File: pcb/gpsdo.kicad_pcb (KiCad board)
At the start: 4 copper layers, 140 x 100 mm, 159 parts, among them IC1 ICE40LP384-SG32, J1 JTAG, J10 CLK0, J11 CLK7, J12 USB_B_Micro, J13 CLK6, J14 CLK5, J15 CLK4, J2 SSD1306, J3 EXT_CLOCK, J4 GPS_ANT, J5 USB_B_Micro, J6 CLK3, J7 Screw_Terminal_01x03, J8 CLK2, J9 CLK1, M1 E73-2G4M08S1C-52840, Q1 S9018, SW1 EC11, SW2 MCML4-112B, U1 MCP9808_MSOP, U2 MCP9808_MSOP, U3 TPS652510, U4 LT1763xS8, U5 74LVC1G17, U6 Si5351C-B-GM, U7 74LVC1G17, U8 uBlox NEO-7M, U9 AD5761R, Y1 32768, Y2 8663-XS

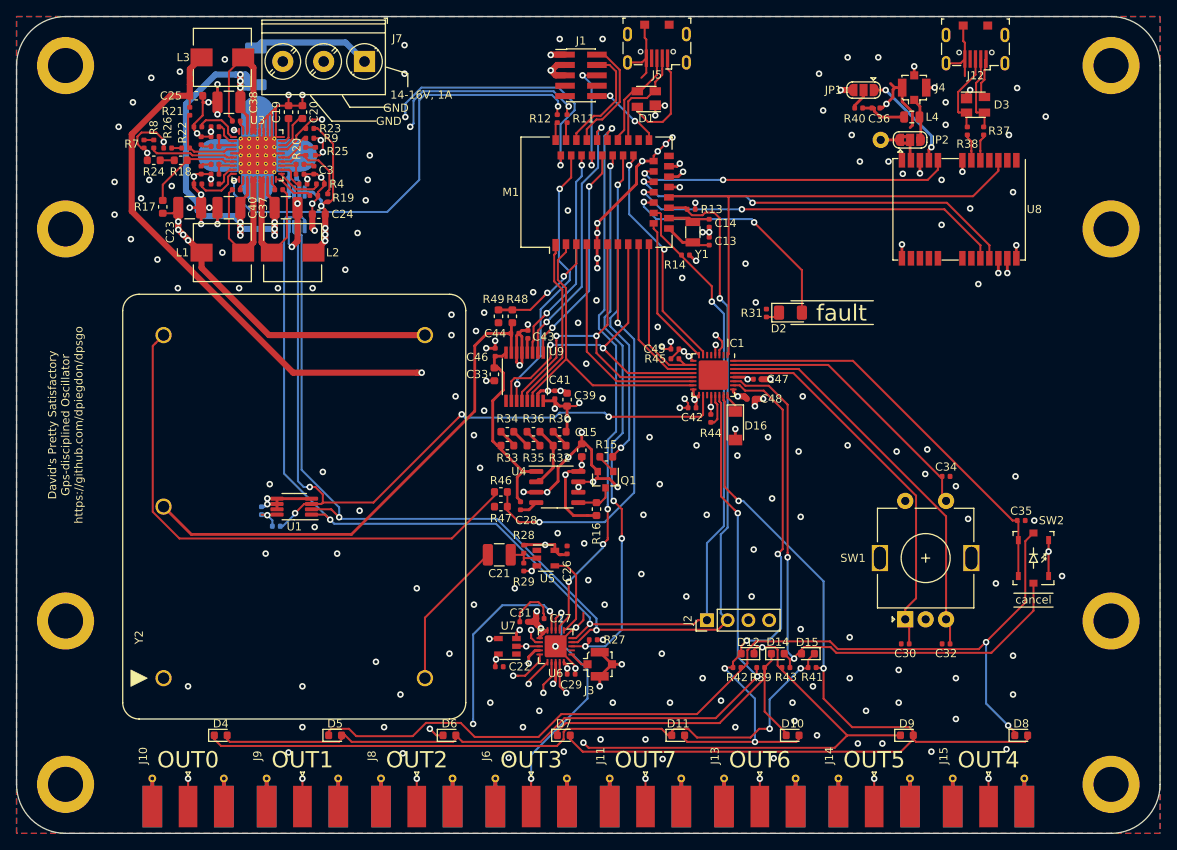
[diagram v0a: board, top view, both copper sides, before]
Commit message: added shield and more silkscreen, cleanup
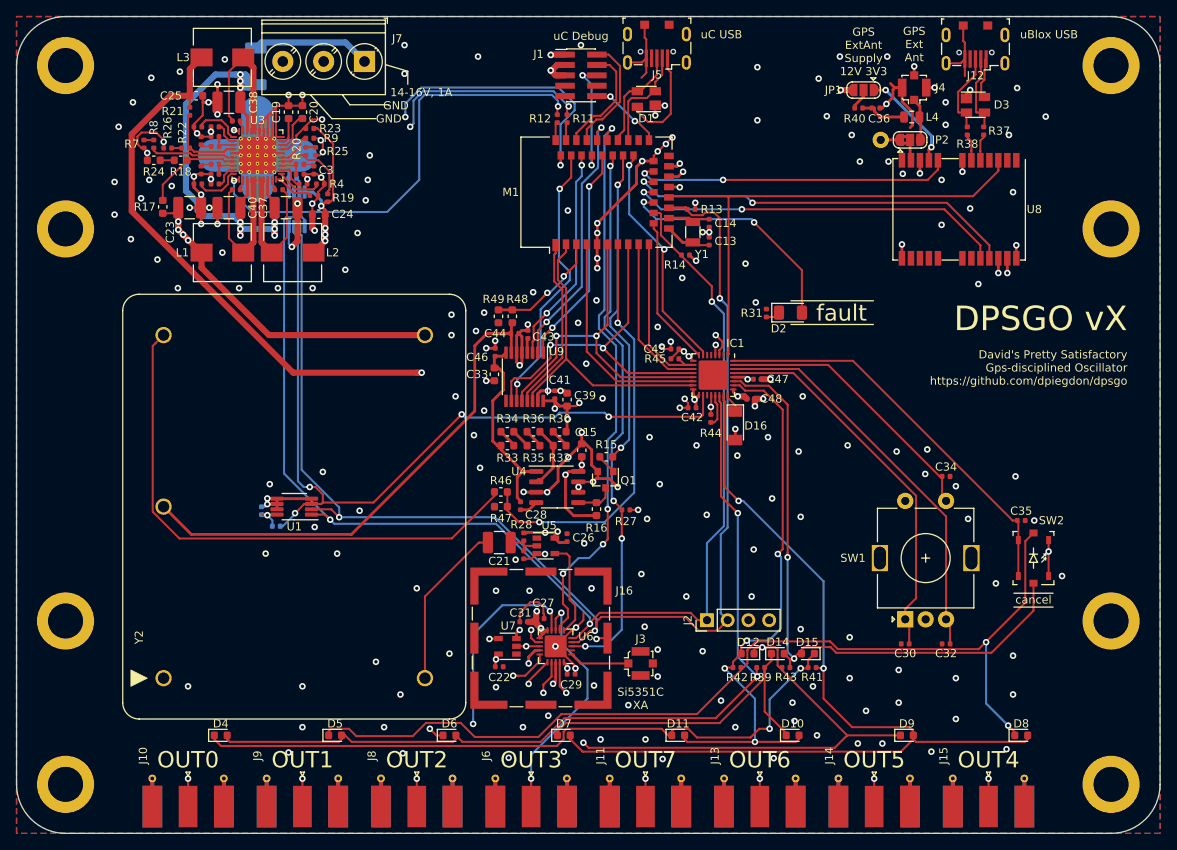
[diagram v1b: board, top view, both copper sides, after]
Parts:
- added J16: RF_Shield_One_Piece, RF_Shielding:Laird_Technologies_BMI-S-202-F_16.50x16.50mm, F.Cu at (94.2, 116.1)
- moved R27 16.4 mm to (104.6, 100.4)
- moved J3 5.00 mm to (106.4, 119.2)
- moved C21 1.50 mm to (89.1, 104.4)
- moved C26 1.50 mm to (97.4, 103.8)
- moved R28 1.50 mm to (92.1, 103.7)
- moved R29 1.50 mm to (92.1, 105.9)
- moved U5 1.50 mm to (94.8, 104.8)
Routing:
- net GND: track 303.1 -> 317.1 mm, vias 220 -> 222
- net Net-(J3-Pad1): track 2.45 -> 7.41 mm
- net /OCXO_OUTPUT: track 18.3 -> 20.4 mm
- net /SCL: track 157.5 -> 159.2 mm
- net /OCXO_DIGITAL: track 10.5 -> 11.9 mm
- net /PLL_EN: track 67.5 -> 68.8 mm
- net /SWDIO: track 14.3 -> 15.5 mm
- net /PLL_INT: track 68.4 -> 67.4 mm
- net /SDA: track 155.1 -> 155.9 mm
- net /UC_USB_D+: track 12.5 -> 13.3 mm
- net +3V3: track 79.3 -> 79.6 mm, vias 29 -> 30
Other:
- board text added: "DPSGO vX"
- board text added: "GPS Ext Ant"
- board text added: "GPS ExtAnt Supply 12V 3V3"
- board text added: "Si5351C XA"
- board text added: "uBlox USB"
- board text added: "uC Debug"
- board text added: "uC USB"

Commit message: more routing cleanup
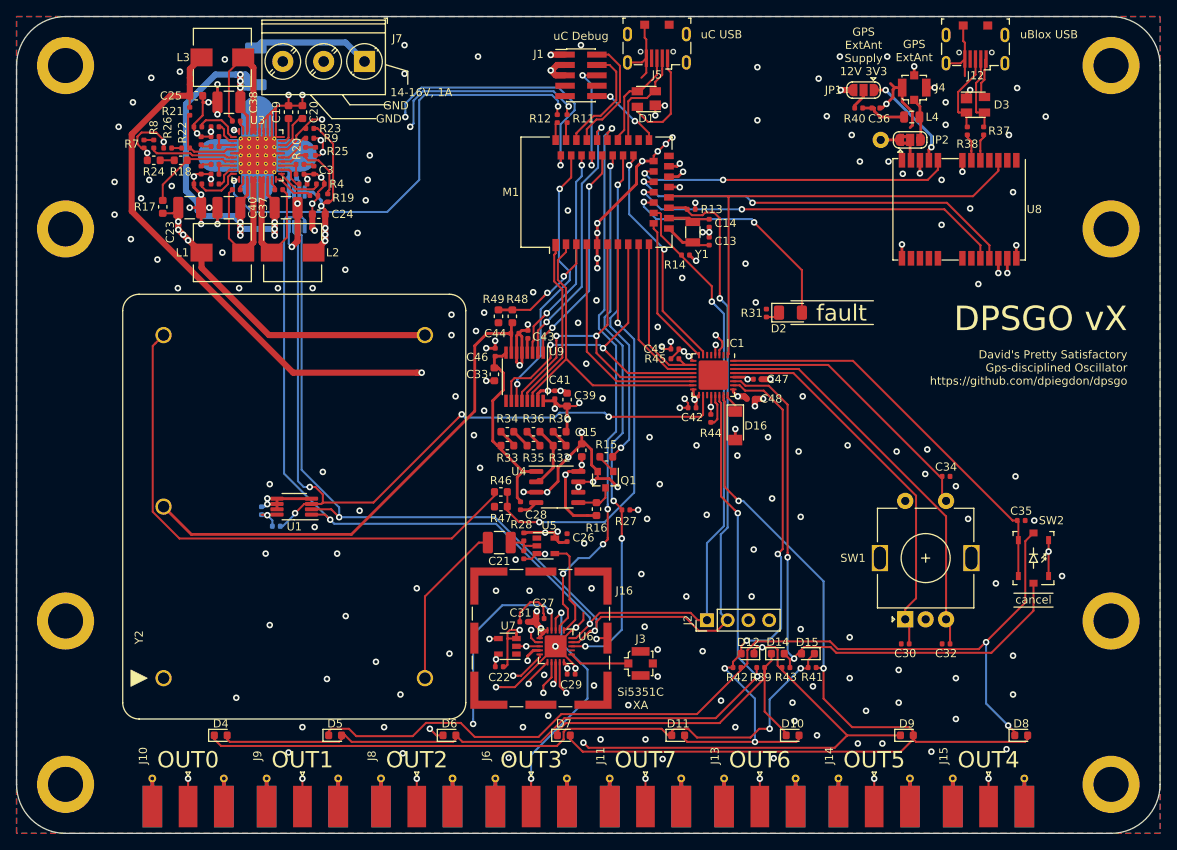
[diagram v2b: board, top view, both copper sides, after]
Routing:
- net GND: track 317.1 -> 333.8 mm, vias 222 -> 225
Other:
- board text added: "GPS ExtAnt"
- board text removed: "GPS Ext Ant"
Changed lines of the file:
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@@
     (thickness 1.6)
     (drawings 38)
-    (tracks 1893)
+    (tracks 1906)
     (zones 0)
     (modules 160)
@@
     (effects (font (size 1 1) (thickness 0.15)))
   )
-  (gr_text "GPS\nExt\nAnt" (at 139.9 43.4) (layer F.SilkS)
+  (gr_text "GPS\nExtAnt" (at 139.9 44.2) (layer F.SilkS)
     (effects (font (size 1 1) (thickness 0.15)))
   )
@@
   (segment (start 97.400001 87.6875) (end 98.5125 87.6875) (width 0.25) (layer F.Cu) (net 2) (status 10))
   (segment (start 98.5125 87.6875) (end 98.9 87.3) (width 0.25) (layer F.Cu) (net 2))
-  (via (at 51 122) (size 0.8) (drill 0.4) (layers F.Cu B.Cu) (net 2))
-  (via (at 65 122) (size 0.8) (drill 0.4) (layers F.Cu B.Cu) (net 2))
+  (via (at 61 114.5) (size 0.8) (drill 0.4) (layers F.Cu B.Cu) (net 2))
+  (via (at 56.9 123.4) (size 0.8) (drill 0.4) (layers F.Cu B.Cu) (net 2))
   (via (at 77 123) (size 0.8) (drill 0.4) (layers F.Cu B.Cu) (net 2))
   (via (at 88.7 122.1) (size 0.8) (drill 0.4) (layers F.Cu B.Cu) (net 2))
@@
   (via (at 86 91.25) (size 0.8) (drill 0.4) (layers F.Cu B.Cu) (net 2))
   (via (at 86.75 95.25) (size 0.8) (drill 0.4) (layers F.Cu B.Cu) (net 2))
-  (via (at 96.25 103.05) (size 0.8) (drill 0.4) (layers F.Cu B.Cu) (net 3))
   (via (at 99.5 104.5) (size 0.8) (drill 0.4) (layers F.Cu B.Cu) (net 2))
   (via (at 107.2 101.5) (size 0.8) (drill 0.4) (layers F.Cu B.Cu) (net 2))
@@
   (via (at 128.2 47.6) (size 0.8) (drill 0.4) (layers F.Cu B.Cu) (net 2))
   (via (at 120.7 52.7) (size 0.8) (drill 0.4) (layers F.Cu B.Cu) (net 2))
+  (segment (start 89.265685 122.1) (end 88.7 122.1) (width 0.25) (layer F.Cu) (net 2))
+  (segment (start 96 117.1) (end 91 122.1) (width 0.25) (layer F.Cu) (net 2))
+  (segment (start 91 122.1) (end 89.265685 122.1) (width 0.25) (layer F.Cu) (net 2))
+  (via (at 94.6 120.6) (size 0.8) (drill 0.4) (layers F.Cu B.Cu) (net 2))
+  (segment (start 90.4 115.1) (end 91.6 115.1) (width 0.25) (layer F.Cu) (net 2))
+  (segment (start 90.1 115.4) (end 90.4 115.1) (width 0.25) (layer F.Cu) (net 2))
+  (segment (start 89.585 119.6) (end 89.88 119.6) (width 0.25) (layer F.Cu) (net 2))
+  (segment (start 89.88 119.6) (end 90.1 119.38) (width 0.25) (layer F.Cu) (net 2))
+  (segment (start 91.2 116.15) (end 90.1 116.15) (width 0.25) (layer F.Cu) (net 2))
+  (segment (start 90.1 119.38) (end 90.1 116.15) (width 0.25) (layer F.Cu) (net 2))
+  (segment (start 90.1 116.15) (end 90.1 115.4) (width 0.25) (layer F.Cu) (net 2))
+  (via (at 68 121.1) (size 0.8) (drill 0.4) (layers F.Cu B.Cu) (net 2))
+  (via (at 70.3 113.4) (size 0.8) (drill 0.4) (layers F.Cu B.Cu) (net 2))
+  (via (at 96.25 103.05) (size 0.8) (drill 0.4) (layers F.Cu B.Cu) (net 3))
   (segment (start 67.7875 67.4625) (end 66.35 68.9) (width 0.75) (layer F.Cu) (net 3) (status 20))
   (via (at 67.3 63.2) (size 0.8) (drill 0.4) (layers F.Cu B.Cu) (net 3))
@@
   (segment (start 67.7875 65.8875) (end 67.7875 66.6875) (width 0.75) (layer F.Cu) (net 3))
   (segment (start 67.7875 64.2) (end 67.7875 65.8875) (width 0.75) (layer F.Cu) (net 3) (status 10))
-  (segment (start 96 121.37468) (end 95.68734 121.68734) (width 0.35) (layer F.Cu) (net 3))
-  (segment (start 96 119.05) (end 96 121.37468) (width 0.35) (layer F.Cu) (net 3) (status 10))
-  (via (at 95.68734 121.68734) (size 0.8) (drill 0.4) (layers F.Cu B.Cu) (net 3))
   (segment (start 97.42501 119.79501) (end 97.42501 119.8) (width 0.35) (layer F.Cu) (net 3))
   (segment (start 97.415 119.785) (end 97.42501 119.79501) (width 0.35) (layer F.Cu) (net 3))
@@
   (via (at 111.2 58) (size 0.8) (drill 0.4) (layers F.Cu B.Cu) (net 3))
   (segment (start 110.87 58.33) (end 111.2 58) (width 0.35) (layer F.Cu) (net 3))
-  (segment (start 94.05 117.6) (end 93.5 117.6) (width 0.35) (layer F.Cu) (net 3) (status 10))
-  (segment (start 93.5 117.6) (end 92.7 118.4) (width 0.35) (layer F.Cu) (net 3))
   (segment (start 93.215 114.1) (end 93.615 113.7) (width 0.75) (layer F.Cu) (net 3) (status 20))
   (segment (start 92.585 114.1) (end 93.215 114.1) (width 0.75) (layer F.Cu) (net 3) (status 10))
@@
   (segment (start 93.615 113.7) (end 93.615 112.885) (width 0.75) (layer F.Cu) (net 3) (status 10))
   (segment (start 93.615 112.885) (end 93.7 112.8) (width 0.75) (layer F.Cu) (net 3))
-  (via (at 92.7 119.2) (size 0.8) (drill 0.4) (layers F.Cu B.Cu) (net 3))
-  (segment (start 92.7 118.4) (end 92.7 119.2) (width 0.35) (layer F.Cu) (net 3))
   (segment (start 97.415 119.465) (end 97 119.05) (width 0.35) (layer F.Cu) (net 3) (status 20))
   (segment (start 94.2 115.3) (end 94.2 114.900004) (width 0.35) (layer F.Cu) (net 3))
@@
   (segment (start 105.085 100.4) (end 106.1 100.4) (width 0.25) (layer F.Cu) (net 3))
   (via (at 106.1 100.4) (size 0.8) (drill 0.4) (layers F.Cu B.Cu) (net 3))
+  (via (at 92.569135 118.869135) (size 0.8) (drill 0.4) (layers F.Cu B.Cu) (net 3))
+  (segment (start 94.05 117.6) (end 93.272585 117.6) (width 0.35) (layer F.Cu) (net 3))
+  (segment (start 92.569135 118.30345) (end 92.569135 118.869135) (width 0.35) (layer F.Cu) (net 3))
+  (segment (start 93.272585 117.6) (end 92.569135 118.30345) (width 0.35) (layer F.Cu) (net 3))
+  (segment (start 96 119.05) (end 96 121.42532) (width 0.35) (layer F.Cu) (net 3))
+  (segment (start 96 121.42532) (end 95.71266 121.71266) (width 0.35) (layer F.Cu) (net 3))
+  (via (at 95.71266 121.71266) (size 0.8) (drill 0.4) (layers F.Cu B.Cu) (net 3))
   (segment (start 52.815 58.1) (end 52.599999 58.315) (width 0.25) (layer F.Cu) (net 4) (status 30))
   (segment (start 53.815 58.1) (end 52.815 58.1) (width 0.25) (layer F.Cu) (net 4) (status 30))
@@
   (segment (start 107 136.72) (end 107 133.3) (width 0.25) (layer F.Cu) (net 79) (status 10))
   (via (at 90.8 120.7) (size 0.8) (drill 0.4) (layers F.Cu B.Cu) (net 79))
-  (segment (start 94.05 118.915685) (end 92.265685 120.7) (width 0.25) (layer F.Cu) (net 79))
-  (segment (start 94.05 118.1) (end 94.05 118.915685) (width 0.25) (layer F.Cu) (net 79) (status 10))
-  (segment (start 92.265685 120.7) (end 91.365685 120.7) (width 0.25) (layer F.Cu) (net 79))
-  (segment (start 91.365685 120.7) (end 90.8 120.7) (width 0.25) (layer F.Cu) (net 79))
   (segment (start 90.3 121.2) (end 90.8 120.7) (width 0.25) (layer In1.Cu) (net 79))
   (segment (start 90.3 126.4) (end 90.3 121.2) (width 0.25) (layer In1.Cu) (net 79))
@@
   (segment (start 107 133.3) (end 105.1 131.4) (width 0.25) (layer In1.Cu) (net 79))
   (segment (start 105.1 131.4) (end 95.3 131.4) (width 0.25) (layer In1.Cu) (net 79))
+  (segment (start 91.76359 120.7) (end 91.365685 120.7) (width 0.25) (layer F.Cu) (net 79))
+  (segment (start 94.05 118.41359) (end 91.76359 120.7) (width 0.25) (layer F.Cu) (net 79))
+  (segment (start 94.05 118.1) (end 94.05 118.41359) (width 0.25) (layer F.Cu) (net 79))
+  (segment (start 91.365685 120.7) (end 90.8 120.7) (width 0.25) (layer F.Cu) (net 79))
   (via (at 121 133.3) (size 0.8) (drill 0.4) (layers F.Cu B.Cu) (net 80))
   (segment (start 121 136.72) (end 121 133.3) (width 0.25) (layer F.Cu) (net 80) (status 10))
   (via (at 92.7 121.7) (size 0.8) (drill 0.4) (layers F.Cu B.Cu) (net 80))
-  (segment (start 95 119.05) (end 92.7 121.35) (width 0.25) (layer F.Cu) (net 80) (status 10))
-  (segment (start 92.7 121.35) (end 92.7 121.7) (width 0.25) (layer F.Cu) (net 80))
   (segment (start 115.4 127.7) (end 121 133.3) (width 0.25) (layer In1.Cu) (net 80))
   (segment (start 95.6 127.7) (end 115.4 127.7) (width 0.25) (layer In1.Cu) (net 80))
   (segment (start 92.7 121.7) (end 92.7 124.8) (width 0.25) (layer In1.Cu) (net 80))
   (segment (start 92.7 124.8) (end 95.6 127.7) (width 0.25) (layer In1.Cu) (net 80))
+  (segment (start 95 119.05) (end 92.7 121.35) (width 0.25) (layer F.Cu) (net 80) (status 10))
+  (segment (start 92.7 121.35) (end 92.7 121.7) (width 0.25) (layer F.Cu) (net 80))
   (via (at 135 133.3) (size 0.8) (drill 0.4) (layers F.Cu B.Cu) (net 81))
   (segment (start 135 136.72) (end 135 133.3) (width 0.25) (layer F.Cu) (net 81) (status 10))
-  (segment (start 94.5 121.801678) (end 94.5 122.8) (width 0.25) (layer F.Cu) (net 81))
   (via (at 94.5 122.8) (size 0.8) (drill 0.4) (layers F.Cu B.Cu) (net 81))
-  (segment (start 95.5 119.05) (end 95.5 120.801678) (width 0.25) (layer F.Cu) (net 81) (status 10))
-  (segment (start 95.5 120.801678) (end 94.5 121.801678) (width 0.25) (layer F.Cu) (net 81))
   (segment (start 94.5 122.8) (end 97 125.3) (width 0.25) (layer In1.Cu) (net 81))
   (segment (start 127 125.3) (end 135 133.3) (width 0.25) (layer In1.Cu) (net 81))
   (segment (start 97 125.3) (end 127 125.3) (width 0.25) (layer In1.Cu) (net 81))
+  (segment (start 95.5 120.9) (end 94.5 121.9) (width 0.25) (layer F.Cu) (net 81))
+  (segment (start 94.5 121.9) (end 94.5 122.8) (width 0.25) (layer F.Cu) (net 81))
+  (segment (start 95.5 119.05) (end 95.5 120.9) (width 0.25) (layer F.Cu) (net 81))
   (via (at 149 133.3) (size 0.8) (drill 0.4) (layers F.Cu B.Cu) (net 82))
   (segment (start 149 136.72) (end 149 133.3) (width 0.25) (layer F.Cu) (net 82) (status 10))

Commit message: PCB v1
more cleanup, release v1
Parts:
- added FID1: Fiducial, Fiducial:Fiducial_1mm_Mask3mm, F.Cu at (43.0, 46.0)
- added FID2: Fiducial, Fiducial:Fiducial_1mm_Mask3mm, F.Cu at (157.0, 46.0)
- added FID3: Fiducial, Fiducial:Fiducial_1mm_Mask3mm, F.Cu at (157.0, 134.0)
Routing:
- net GND: track 333.8 -> 449.6 mm
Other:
- board text added: "DPSGO v1"
- board text removed: "DPSGO vX"

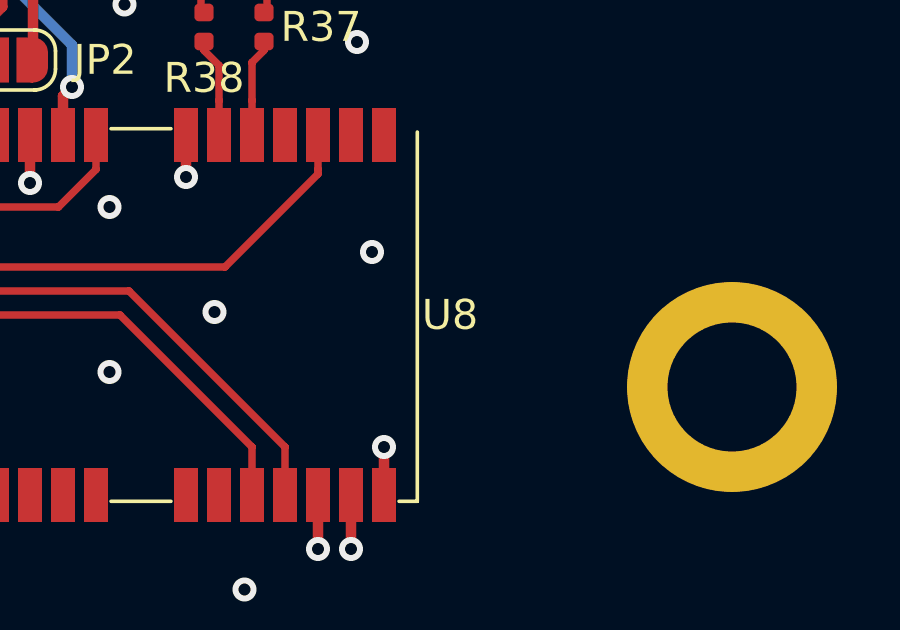
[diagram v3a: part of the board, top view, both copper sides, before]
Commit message: fix missing PAD23 of ublox neo in paste layer (thanks to JLCPCB for spotting this!)
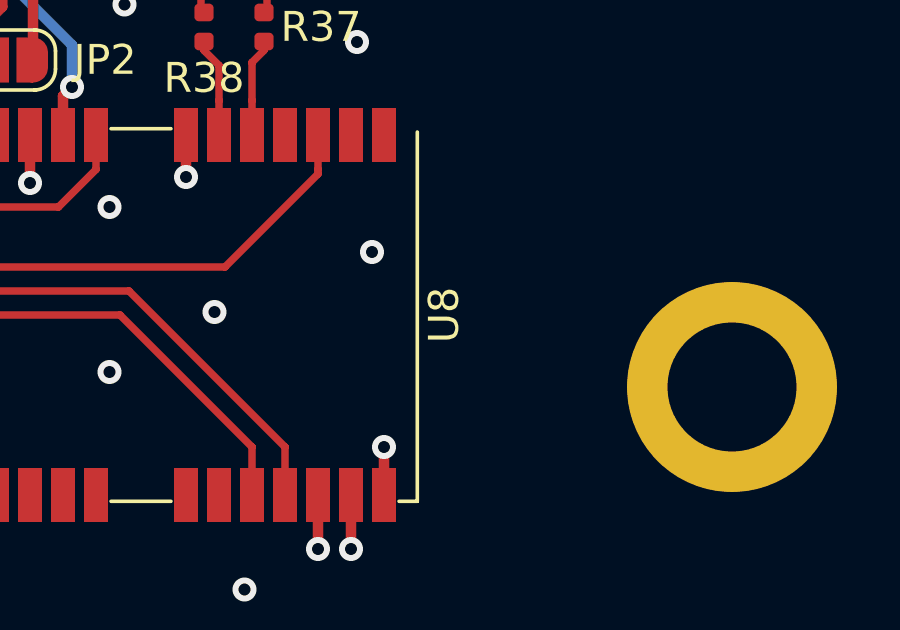
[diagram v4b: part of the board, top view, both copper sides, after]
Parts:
- U8: footprint RF_GPS:ublox_NEO -> dpiegdon:ublox_NEO_fixed_23
